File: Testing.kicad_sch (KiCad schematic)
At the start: 6 parts, among them J1 Conn_01x05_Male

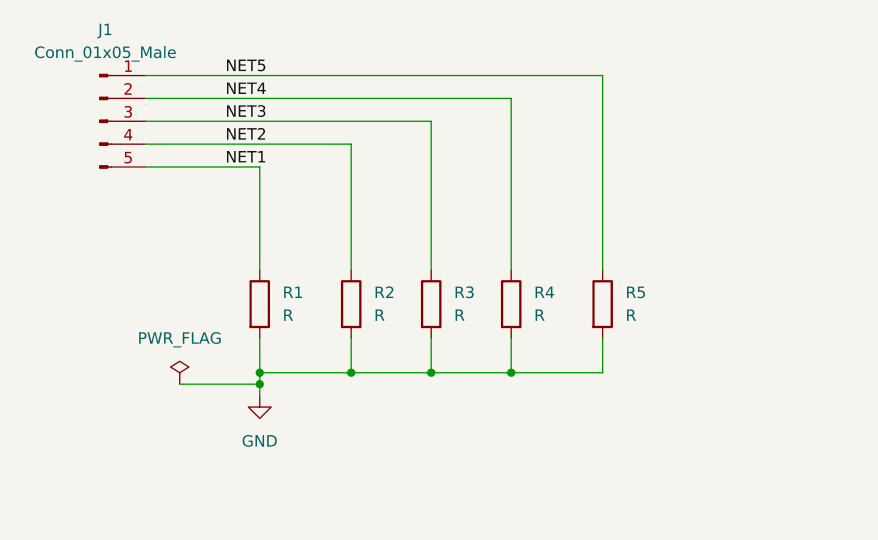
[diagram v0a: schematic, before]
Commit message: Added a Capacitor
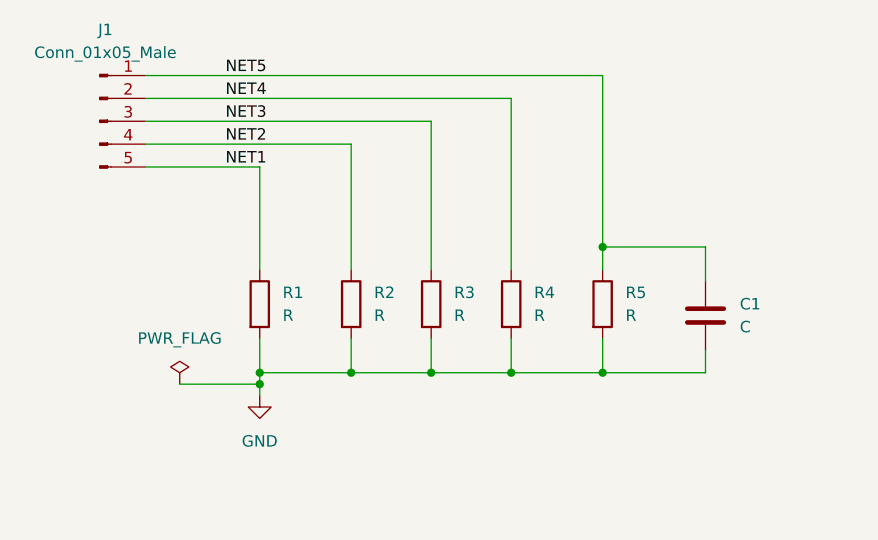
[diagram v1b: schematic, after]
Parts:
- added C1: C, symbol Device:C
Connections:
- net GND: now also C1.2
- net NET5: now also C1.1
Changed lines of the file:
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@@
 (kicad_sch (version 20211123) (generator eeschema)
   (paper "A4")
+  (junction (at 127 60.96) (diameter 0) (color 0 0 0 0)
+  )
   (junction (at 88.9 74.93) (diameter 0) (color 0 0 0 0)
   )
@@
   (junction (at 99.06 74.93) (diameter 0) (color 0 0 0 0)
   )
+  (junction (at 127 74.93) (diameter 0) (color 0 0 0 0)
+  )
   (junction (at 107.95 74.93) (diameter 0) (color 0 0 0 0)
   )
+  (wire (pts (xy 127 60.96) (xy 127 63.5))
+    (stroke (width 0) (type default) (color 0 0 0 0))
+  )
   (wire (pts (xy 88.9 71.12) (xy 88.9 74.93))
     (stroke (width 0) (type default) (color 0 0 0 0))
@@
     (stroke (width 0) (type default) (color 0 0 0 0))
   )
-  (wire (pts (xy 127 41.91) (xy 127 63.5))
+  (wire (pts (xy 127 41.91) (xy 127 60.96))
     (stroke (width 0) (type default) (color 0 0 0 0))
   )
@@
     (stroke (width 0) (type default) (color 0 0 0 0))
   )
+  (wire (pts (xy 138.43 74.93) (xy 127 74.93))
+    (stroke (width 0) (type default) (color 0 0 0 0))
+  )
   (wire (pts (xy 88.9 76.2) (xy 88.9 77.47))
     (stroke (width 0) (type default) (color 0 0 0 0))
@@
     (stroke (width 0) (type default) (color 0 0 0 0))
   )
+  (wire (pts (xy 138.43 72.39) (xy 138.43 74.93))
+    (stroke (width 0) (type default) (color 0 0 0 0))
+  )
+  (wire (pts (xy 138.43 60.96) (xy 127 60.96))
+    (stroke (width 0) (type default) (color 0 0 0 0))
+  )
   (wire (pts (xy 76.2 44.45) (xy 116.84 44.45))
     (stroke (width 0) (type default) (color 0 0 0 0))
@@
   )
   (wire (pts (xy 76.2 46.99) (xy 107.95 46.99))
+    (stroke (width 0) (type default) (color 0 0 0 0))
+  )
+  (wire (pts (xy 138.43 64.77) (xy 138.43 60.96))
     (stroke (width 0) (type default) (color 0 0 0 0))
   )
@@
     (pin "2")
   )
+  (symbol (lib_id "Device:C") (at 138.43 68.58 0) (unit 1)
+    (in_bom yes) (on_board yes) (fields_autoplaced)
+    (property "Reference" "C1" (id 0) (at 142.24 67.3099 0)
+      (effects (font (size 1.27 1.27)) (justify left))
+    )
+    (property "Value" "C" (id 1) (at 142.24 69.8499 0)
+      (effects (font (size 1.27 1.27)) (justify left))
+    )
+    (property "Footprint" "" (id 2) (at 139.3952 72.39 0)
+      (effects (font (size 1.27 1.27)) hide)
+    )
+    (property "Datasheet" "~" (id 3) (at 138.43 68.58 0)
+      (effects (font (size 1.27 1.27)) hide)
+    )
+    (pin "1")
+    (pin "2")
+  )
   (symbol (lib_id "Device:R") (at 107.95 67.31 0) (unit 1)
     (in_bom yes) (on_board yes) (fields_autoplaced)
@@
       (reference "#PWR01") (unit 1) (value "GND") (footprint "")
     )
+    (path "/ebe81818-1aef-4caa-b041-34931f38d846"
+      (reference "C1") (unit 1) (value "C") (footprint "")
+    )
     (path "/232a1eaa-ce33-4943-a6f5-1a5ebae06687"

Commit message: Added 2nd Capacitor.
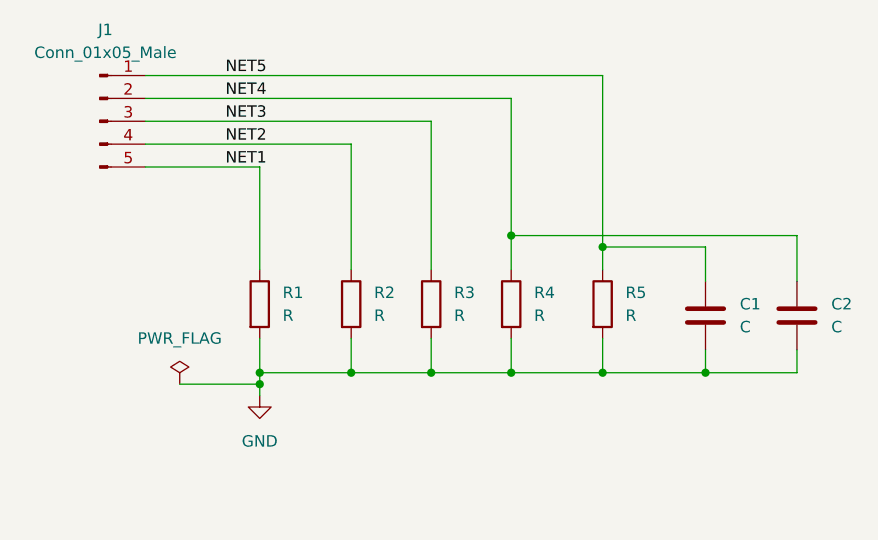
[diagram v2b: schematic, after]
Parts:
- added C2: C, symbol Device:C
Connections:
- net GND: now also C2.2
- net NET4: now also C2.1
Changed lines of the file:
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@@
   (junction (at 88.9 74.93) (diameter 0) (color 0 0 0 0)
   )
+  (junction (at 116.84 59.69) (diameter 0) (color 0 0 0 0)
+  )
   (junction (at 116.84 74.93) (diameter 0) (color 0 0 0 0)
   )
   (junction (at 88.9 76.2) (diameter 0) (color 0 0 0 0)
   )
+  (junction (at 138.43 74.93) (diameter 0) (color 0 0 0 0)
+  )
   (junction (at 99.06 74.93) (diameter 0) (color 0 0 0 0)
   )
@@
     (stroke (width 0) (type default) (color 0 0 0 0))
   )
+  (wire (pts (xy 148.59 59.69) (xy 116.84 59.69))
+    (stroke (width 0) (type default) (color 0 0 0 0))
+  )
   (wire (pts (xy 127 71.12) (xy 127 74.93))
     (stroke (width 0) (type default) (color 0 0 0 0))
@@
     (stroke (width 0) (type default) (color 0 0 0 0))
   )
+  (wire (pts (xy 148.59 72.39) (xy 148.59 74.93))
+    (stroke (width 0) (type default) (color 0 0 0 0))
+  )
   (wire (pts (xy 116.84 74.93) (xy 107.95 74.93))
     (stroke (width 0) (type default) (color 0 0 0 0))
   )
+  (wire (pts (xy 116.84 59.69) (xy 116.84 63.5))
+    (stroke (width 0) (type default) (color 0 0 0 0))
+  )
   (wire (pts (xy 76.2 41.91) (xy 127 41.91))
     (stroke (width 0) (type default) (color 0 0 0 0))
@@
     (stroke (width 0) (type default) (color 0 0 0 0))
   )
+  (wire (pts (xy 148.59 74.93) (xy 138.43 74.93))
+    (stroke (width 0) (type default) (color 0 0 0 0))
+  )
   (wire (pts (xy 138.43 60.96) (xy 127 60.96))
     (stroke (width 0) (type default) (color 0 0 0 0))
@@
     (stroke (width 0) (type default) (color 0 0 0 0))
   )
-  (wire (pts (xy 116.84 44.45) (xy 116.84 63.5))
+  (wire (pts (xy 116.84 44.45) (xy 116.84 59.69))
     (stroke (width 0) (type default) (color 0 0 0 0))
   )
@@
   )
   (wire (pts (xy 99.06 49.53) (xy 99.06 63.5))
+    (stroke (width 0) (type default) (color 0 0 0 0))
+  )
+  (wire (pts (xy 148.59 64.77) (xy 148.59 59.69))
     (stroke (width 0) (type default) (color 0 0 0 0))
   )
@@
     (pin "1")
   )
+  (symbol (lib_id "Device:C") (at 148.59 68.58 0) (unit 1)
+    (in_bom yes) (on_board yes) (fields_autoplaced)
+    (property "Reference" "C2" (id 0) (at 152.4 67.3099 0)
+      (effects (font (size 1.27 1.27)) (justify left))
+    )
+    (property "Value" "C" (id 1) (at 152.4 69.8499 0)
+      (effects (font (size 1.27 1.27)) (justify left))
+    )
+    (property "Footprint" "" (id 2) (at 149.5552 72.39 0)
+      (effects (font (size 1.27 1.27)) hide)
+    )
+    (property "Datasheet" "~" (id 3) (at 148.59 68.58 0)
+      (effects (font (size 1.27 1.27)) hide)
+    )
+    (pin "1")
+    (pin "2")
+  )
   (symbol (lib_id "Device:R") (at 99.06 67.31 0) (unit 1)
     (in_bom yes) (on_board yes) (fields_autoplaced)
@@
       (reference "C1") (unit 1) (value "C") (footprint "")
     )
+    (path "/7580d9ad-efbd-47cc-ab60-7512e1dc5e85"
+      (reference "C2") (unit 1) (value "C") (footprint "")
+    )
     (path "/232a1eaa-ce33-4943-a6f5-1a5ebae06687"

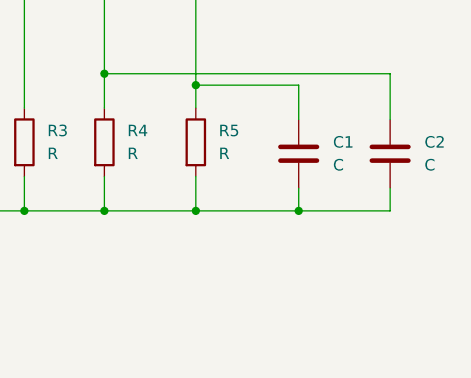
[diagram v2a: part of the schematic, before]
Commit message: Added a Diode.
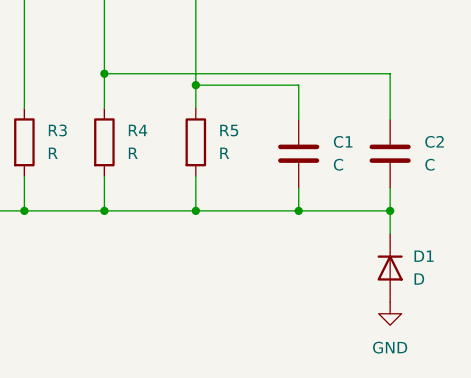
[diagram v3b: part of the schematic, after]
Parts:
- added D1: D, symbol Device:D
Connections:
- net GND: now also D1.1 (K), D1.2 (A)
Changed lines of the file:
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@@
   (junction (at 127 60.96) (diameter 0) (color 0 0 0 0)
   )
+  (junction (at 148.59 74.93) (diameter 0) (color 0 0 0 0)
+  )
   (junction (at 88.9 74.93) (diameter 0) (color 0 0 0 0)
   )
@@
   )
   (wire (pts (xy 148.59 74.93) (xy 138.43 74.93))
+    (stroke (width 0) (type default) (color 0 0 0 0))
+  )
+  (wire (pts (xy 148.59 74.93) (xy 148.59 77.47))
     (stroke (width 0) (type default) (color 0 0 0 0))
   )
@@
     (pin "2")
   )
+  (symbol (lib_id "Device:D") (at 148.59 81.28 270) (unit 1)
+    (in_bom yes) (on_board yes) (fields_autoplaced)
+    (property "Reference" "D1" (id 0) (at 151.13 80.0099 90)
+      (effects (font (size 1.27 1.27)) (justify left))
+    )
+    (property "Value" "D" (id 1) (at 151.13 82.5499 90)
+      (effects (font (size 1.27 1.27)) (justify left))
+    )
+    (property "Footprint" "" (id 2) (at 148.59 81.28 0)
+      (effects (font (size 1.27 1.27)) hide)
+    )
+    (property "Datasheet" "~" (id 3) (at 148.59 81.28 0)
+      (effects (font (size 1.27 1.27)) hide)
+    )
+    (pin "1")
+    (pin "2")
+  )
+  (symbol (lib_id "power:GND") (at 148.59 85.09 0) (unit 1)
+    (in_bom yes) (on_board yes) (fields_autoplaced)
+    (property "Reference" "#PWR?" (id 0) (at 148.59 91.44 0)
+      (effects (font (size 1.27 1.27)) hide)
+    )
+    (property "Value" "GND" (id 1) (at 148.59 90.17 0))
+    (property "Footprint" "" (id 2) (at 148.59 85.09 0)
+      (effects (font (size 1.27 1.27)) hide)
+    )
+    (property "Datasheet" "" (id 3) (at 148.59 85.09 0)
+      (effects (font (size 1.27 1.27)) hide)
+    )
+    (pin "1")
+  )
   (symbol (lib_id "Device:C") (at 138.43 68.58 0) (unit 1)
     (in_bom yes) (on_board yes) (fields_autoplaced)
@@
       (reference "#PWR01") (unit 1) (value "GND") (footprint "")
     )
+    (path "/d338041e-f043-4bf8-9207-4861a0250c4a"
+      (reference "#PWR?") (unit 1) (value "GND") (footprint "")
+    )
     (path "/ebe81818-1aef-4caa-b041-34931f38d846"
       (reference "C1") (unit 1) (value "C") (footprint "")
@@
       (reference "C2") (unit 1) (value "C") (footprint "")
     )
+    (path "/b2beffe4-de35-4c24-8dfc-75720d58e4d8"
+      (reference "D1") (unit 1) (value "D") (footprint "")
+    )
     (path "/232a1eaa-ce33-4943-a6f5-1a5ebae06687"

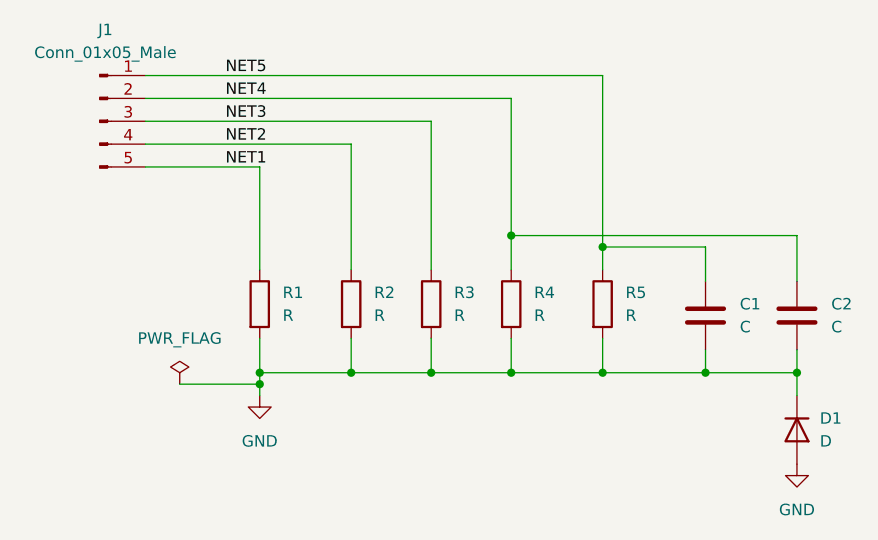
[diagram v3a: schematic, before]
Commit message: Update Testing.kicad_sch
Change NET LABEL 5 to 9999
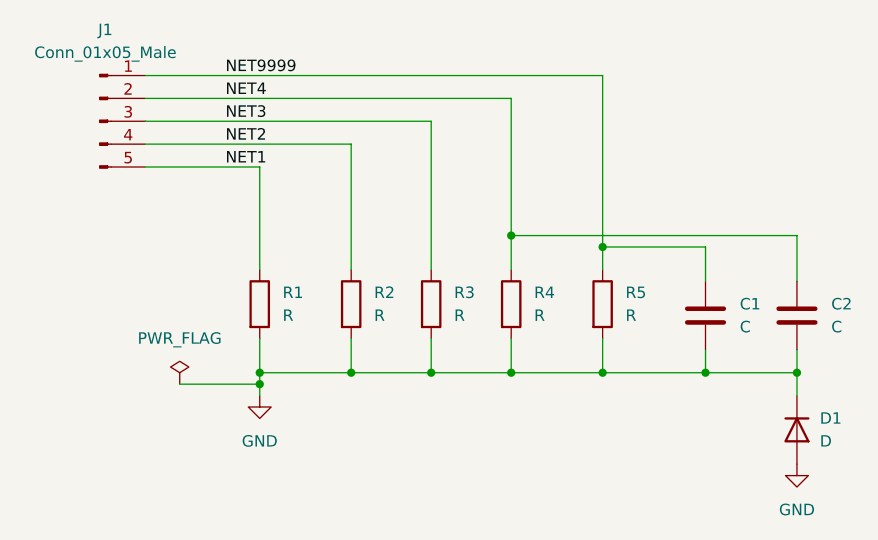
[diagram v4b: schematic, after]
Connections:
- net NET5 renamed NET9999
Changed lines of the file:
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@@
     (stroke (width 0) (type default) (color 0 0 0 0))
   )
-  (label "NET5" (at 85.09 41.91 0)
+  (label "NET9999" (at 85.09 41.91 0)
     (effects (font (size 1.27 1.27)) (justify left bottom))
   )
